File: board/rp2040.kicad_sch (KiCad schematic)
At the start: 22 parts, among them U1 W25Q128JVS, U2 RP2040, Y1 12MhZ

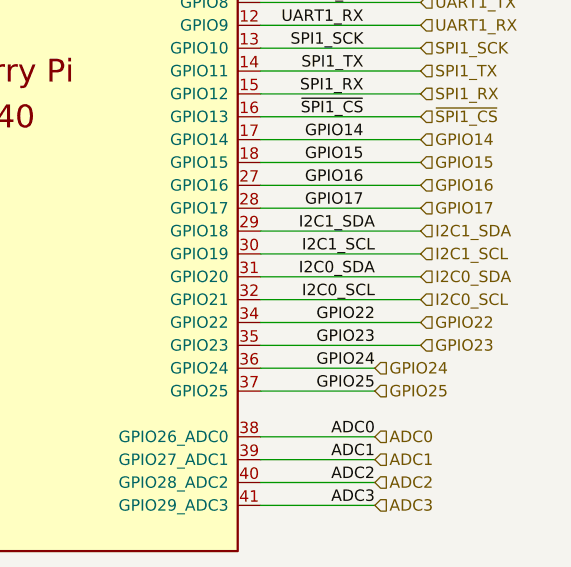
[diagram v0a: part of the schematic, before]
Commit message: changed top I2C connector to be a UNIO connector for a mac address chip
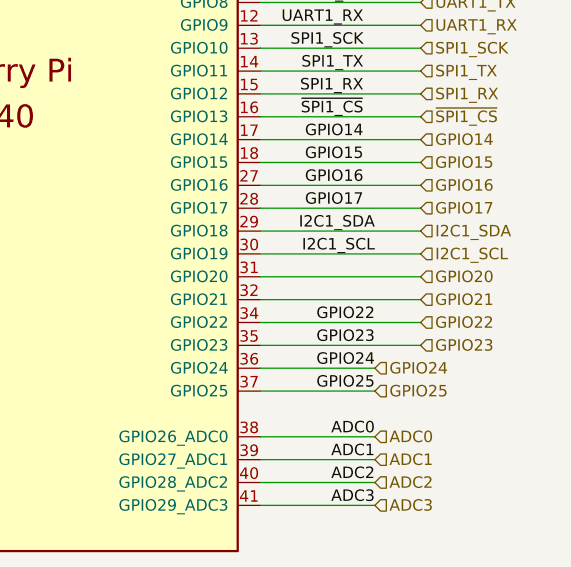
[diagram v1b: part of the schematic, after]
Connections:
- net I2C0_SCL renamed GPIO21
- net I2C0_SDA renamed GPIO20
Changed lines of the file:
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@@
-    (effects (font (size 1.27 1.27)) (justify right bottom))
-  )
-  (label "I2C0_SCL" (at 177.8 129.54 180)
     (effects (font (size 1.27 1.27)) (justify right bottom))
   )
@@
   )
   (label "SPI0_SCK" (at 176.53 81.28 180)
-    (effects (font (size 1.27 1.27)) (justify right bottom))
-  )
-  (label "I2C0_SDA" (at 177.8 127 180)
     (effects (font (size 1.27 1.27)) (justify right bottom))
   )
@@
     (effects (font (size 1.27 1.27)) (justify left))
   )
-  (hierarchical_label "I2C0_SCL" (shape input) (at 182.88 129.54 0)
+  (hierarchical_label "GPIO21" (shape input) (at 182.88 129.54 0)
     (effects (font (size 1.27 1.27)) (justify left))
   )
@@
     (effects (font (size 1.27 1.27)) (justify left))
   )
-  (hierarchical_label "I2C0_SDA" (shape input) (at 182.88 127 0)
+  (hierarchical_label "GPIO20" (shape input) (at 182.88 127 0)
     (effects (font (size 1.27 1.27)) (justify left))
   )

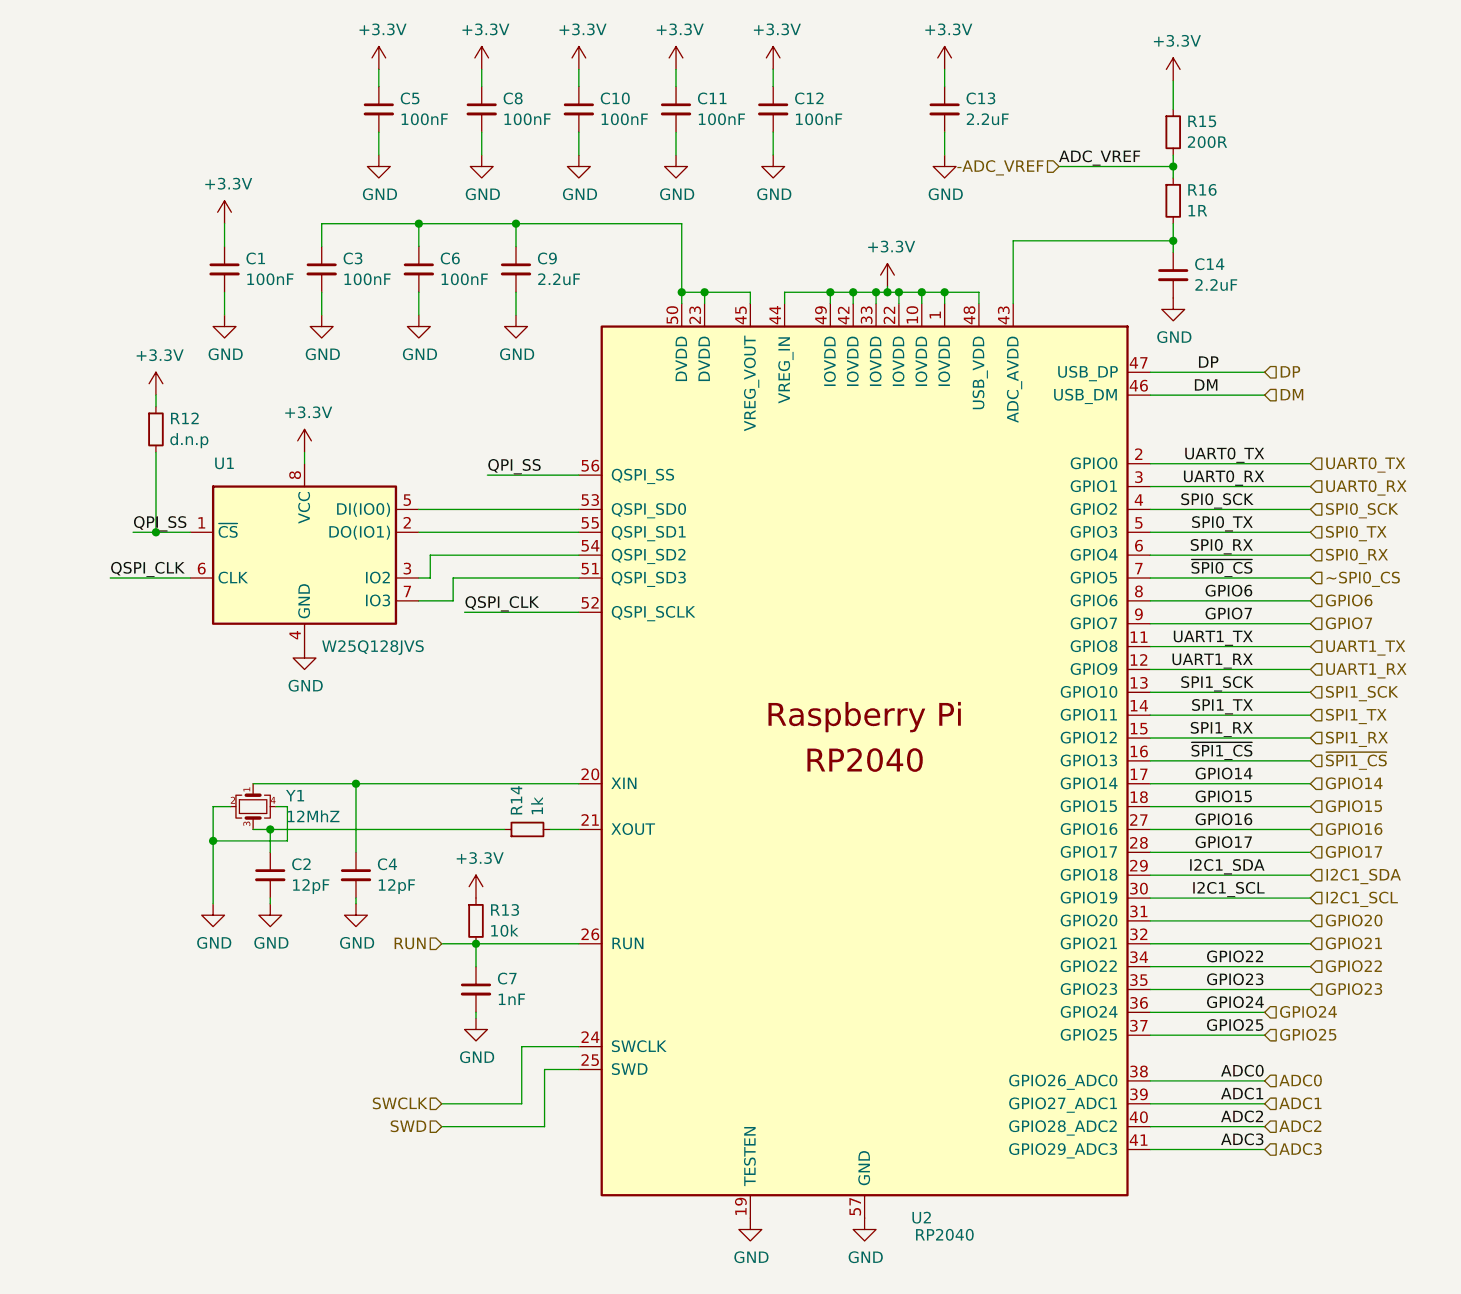
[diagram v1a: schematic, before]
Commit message: changed power symbols in subsheets
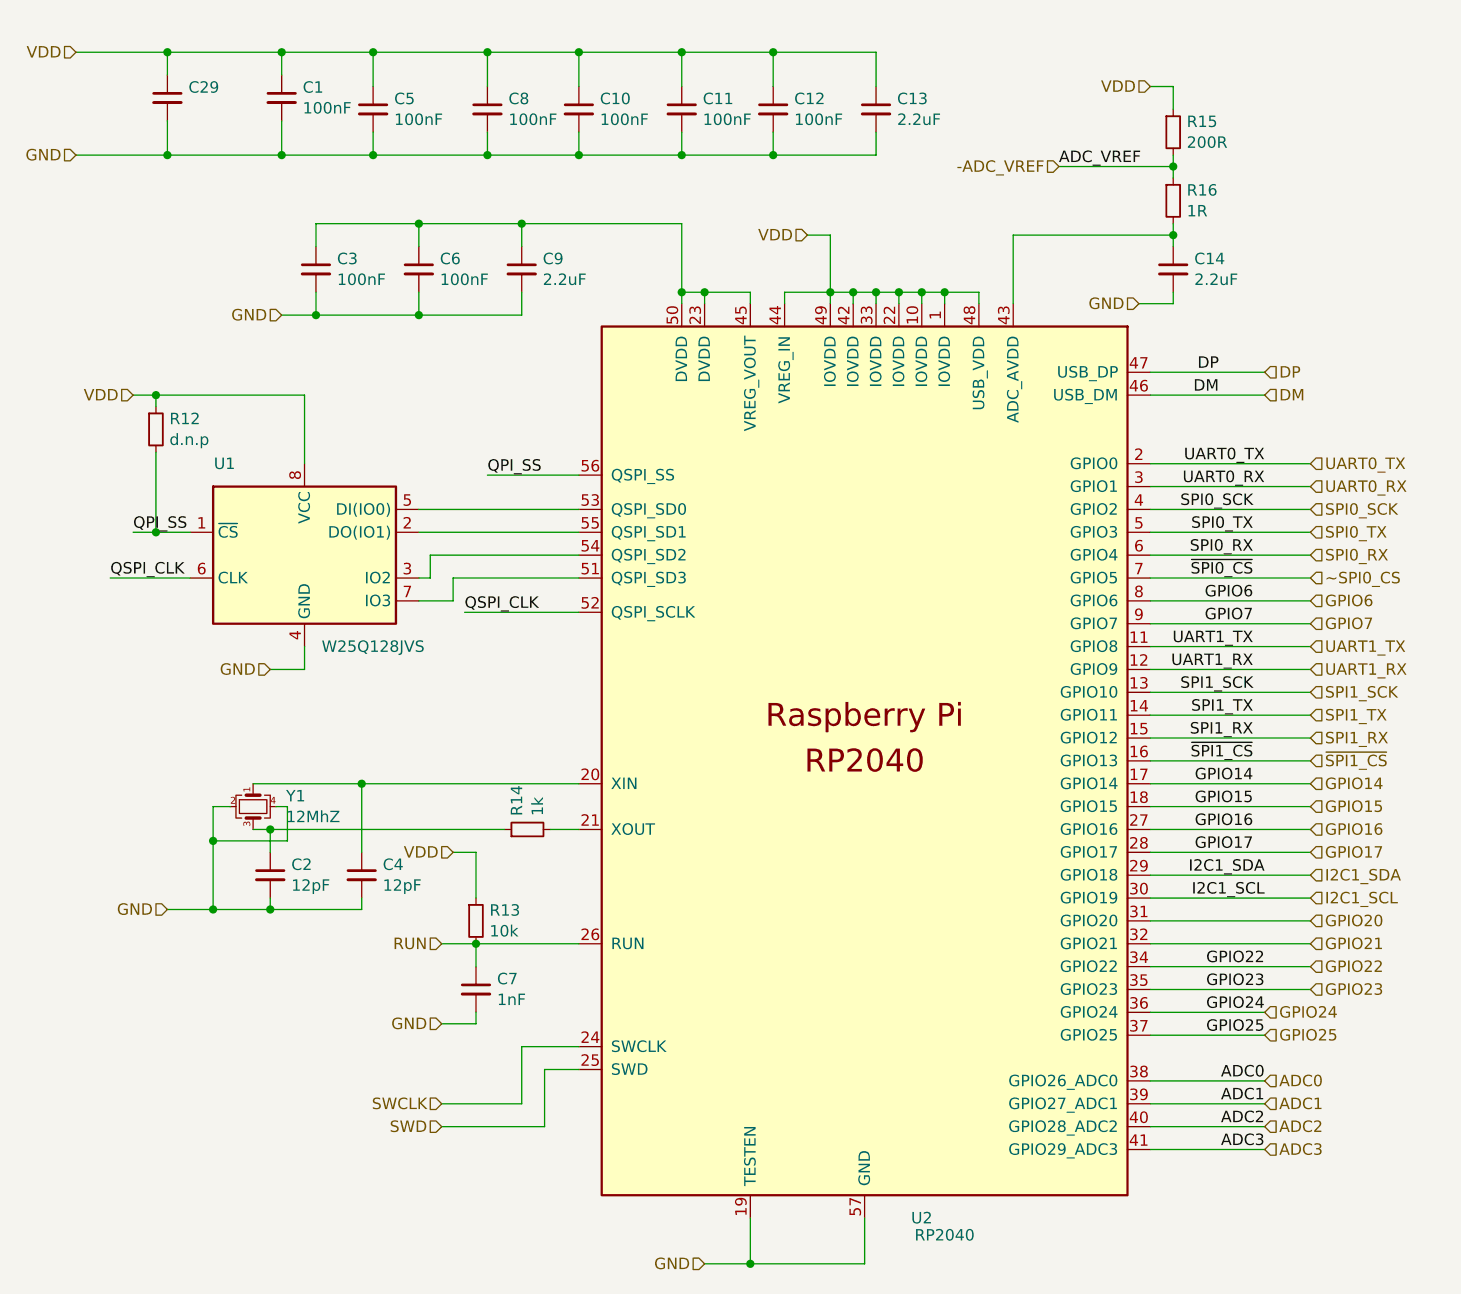
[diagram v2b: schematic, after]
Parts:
- added C29: (no value), symbol Device:C_Small
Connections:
- net GND: now also C29.2
- net +3V3 renamed VDD
- net VDD: now also C29.1
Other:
- moved on the sheet: C1, C11, C13, C14, C3, C4, C5, C8, C9

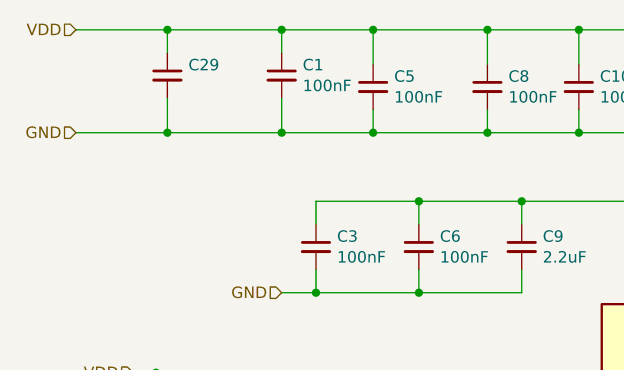
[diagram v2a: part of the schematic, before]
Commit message: updated connector footprints and added planes
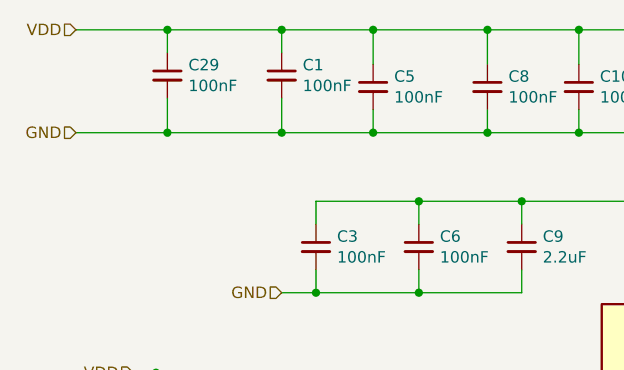
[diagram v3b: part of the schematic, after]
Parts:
- C29: value (none) -> 100nF; footprint (none) -> Capacitor_SMD:C_0603_1608Metric
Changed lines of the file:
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@@
       (effects (font (size 1.27 1.27)) (justify left))
     )
-    (property "Value" "" (id 1) (at 58.2168 36.703 0)
+    (property "Value" "100nF" (id 1) (at 58.2168 36.703 0)
       (effects (font (size 1.27 1.27)) (justify left))
     )
-    (property "Footprint" "" (id 2) (at 55.88 35.56 0)
+    (property "Footprint" "Capacitor_SMD:C_0603_1608Metric" (id 2) (at 55.88 35.56 0)
       (effects (font (size 1.27 1.27)) hide)
     )

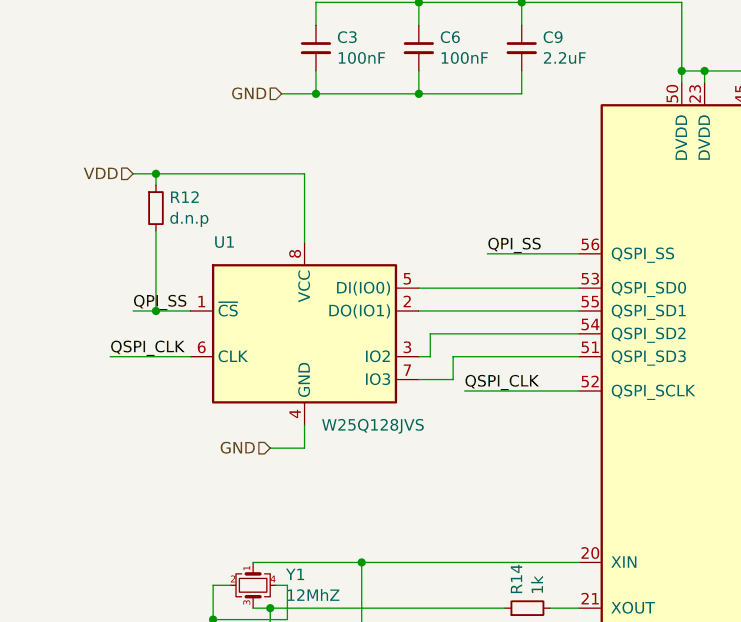
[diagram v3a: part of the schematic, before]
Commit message: upgraded to new kicad and switched to standard flash
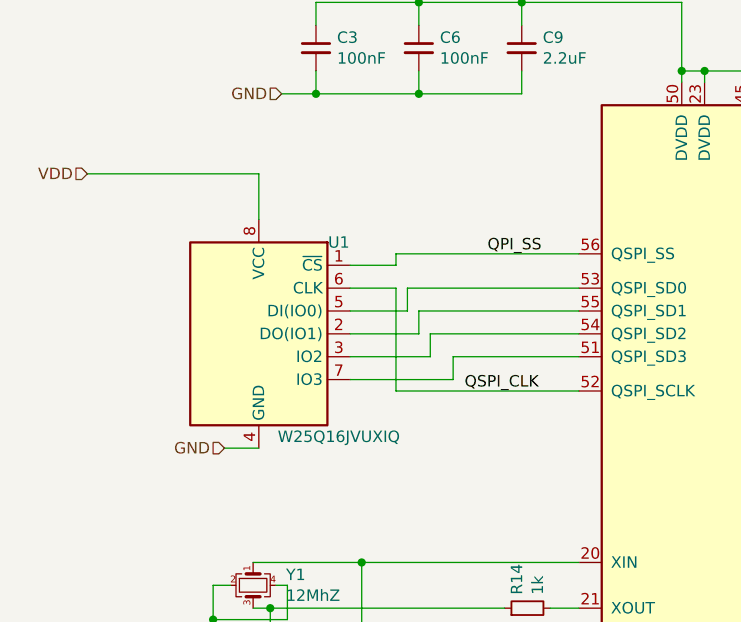
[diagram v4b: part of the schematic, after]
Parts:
- removed R12: d.n.p, Resistor_SMD:R_0603_1608Metric, symbol Device:R_Small
- U1: value W25Q128JVS -> W25Q16JVUXIQ; footprint Package_SO:SOIC-8_5.23x5.23mm_P1.27mm -> Package_DFN_QFN:DFN-8-1EP_3x2mm_P0.5mm_EP1.3x1.5mm
- U2: footprint b018:RP2040-QFN-56 -> Package_DFN_QFN:QFN-56-1EP_7x7mm_P0.4mm_EP3.2x3.2mm
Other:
- moved on the sheet: U1

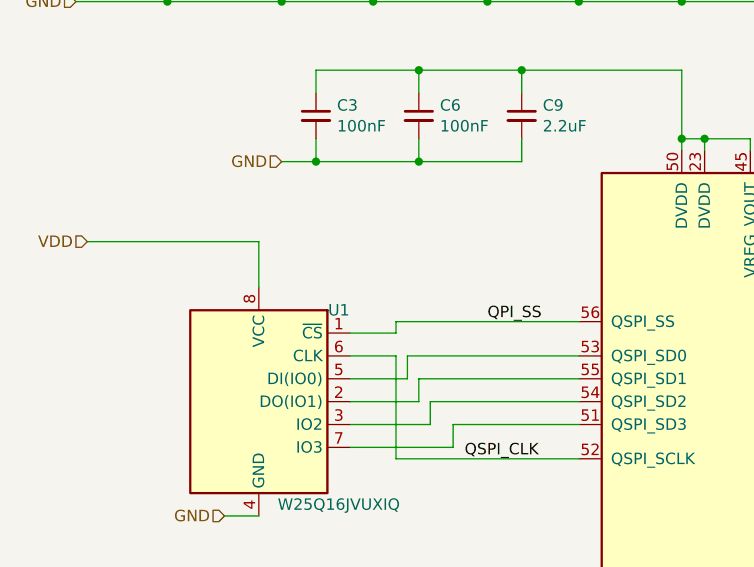
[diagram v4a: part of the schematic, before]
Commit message: updated I2C to fixed pinning
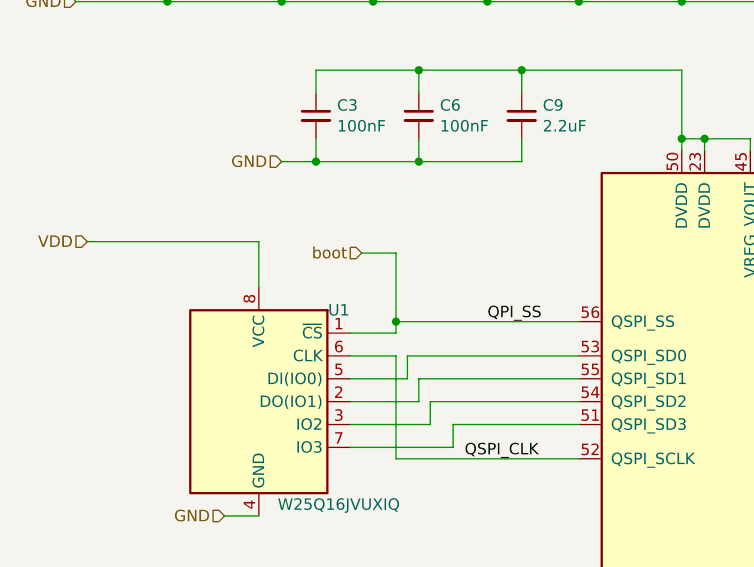
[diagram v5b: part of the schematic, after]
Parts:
- U2: footprint Package_DFN_QFN:QFN-56-1EP_7x7mm_P0.4mm_EP3.2x3.2mm -> RP2040_minimal:RP2040-QFN-56
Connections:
- net QPI_SS renamed boot
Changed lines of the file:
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@@
   (junction (at 113.03 57.15) (diameter 0) (color 0 0 0 0)
   )
+  (junction (at 81.28 77.47) (diameter 0) (color 0 0 0 0)
+  )
   (junction (at 60.96 118.11) (diameter 0) (color 0 0 0 0)
   )
@@
     (stroke (width 0) (type default))
   )
+  (wire (pts (xy 77.47 69.85) (xy 81.28 69.85))
+    (stroke (width 0) (type default))
+  )
   (wire (pts (xy 113.03 41.91) (xy 123.19 41.91))
     (stroke (width 0) (type default))
@@
   )
   (wire (pts (xy 68.58 59.69) (xy 72.39 59.69))
+    (stroke (width 0) (type default))
+  )
+  (wire (pts (xy 81.28 69.85) (xy 81.28 77.47))
     (stroke (width 0) (type default))
   )
@@
   (hierarchical_label "GPIO20" (shape input) (at 182.88 127 0) (fields_autoplaced)
     (effects (font (size 1.27 1.27)) (justify left))
+  )
+  (hierarchical_label "boot" (shape input) (at 77.47 69.85 180) (fields_autoplaced)
+    (effects (font (size 1.27 1.27)) (justify right))
   )
   (hierarchical_label "SPI0_RX" (shape input) (at 182.88 86.36 0) (fields_autoplaced)
@@
       (effects (font (size 1.27 1.27)))
     )
-    (property "Footprint" "Package_DFN_QFN:QFN-56-1EP_7x7mm_P0.4mm_EP3.2x3.2mm" (at 114.3 109.22 0)
-      (effects (font (size 1.27 1.27)) hide)
-    )
+    (property "Footprint" "RP2040_minimal:RP2040-QFN-56" (at 114.3 109.22 0)
+      (effects (font (size 1.27 1.27)) hide)
+    )
